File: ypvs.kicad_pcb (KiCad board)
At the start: 2 copper layers, 17 parts, among them J1 Servo, J2 LM_2596 _Input, J3 HV_Cable, J4 Motorcycle Battery, U1 Stm32f103_BluePill, U2 LM1117-3.3, U3 H11L1

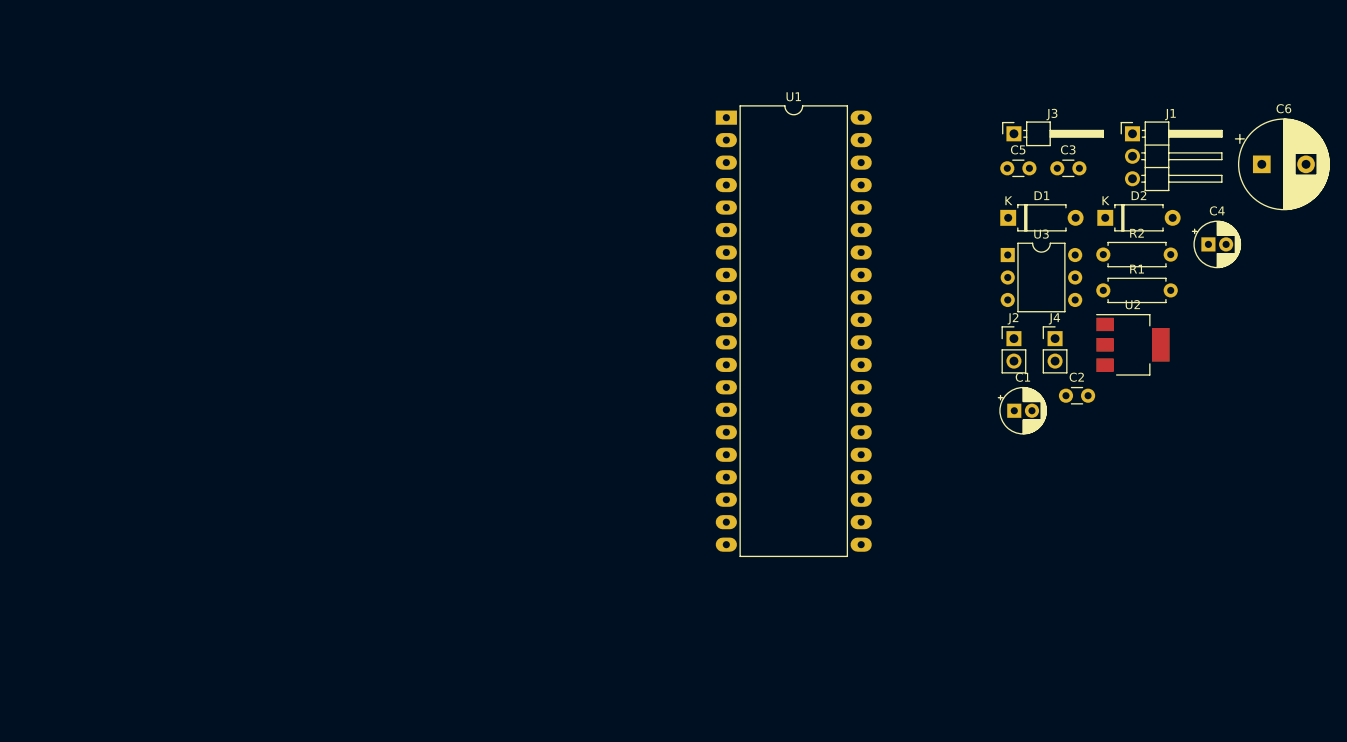
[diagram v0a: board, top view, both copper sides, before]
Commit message: added pcb outline and mounting holes
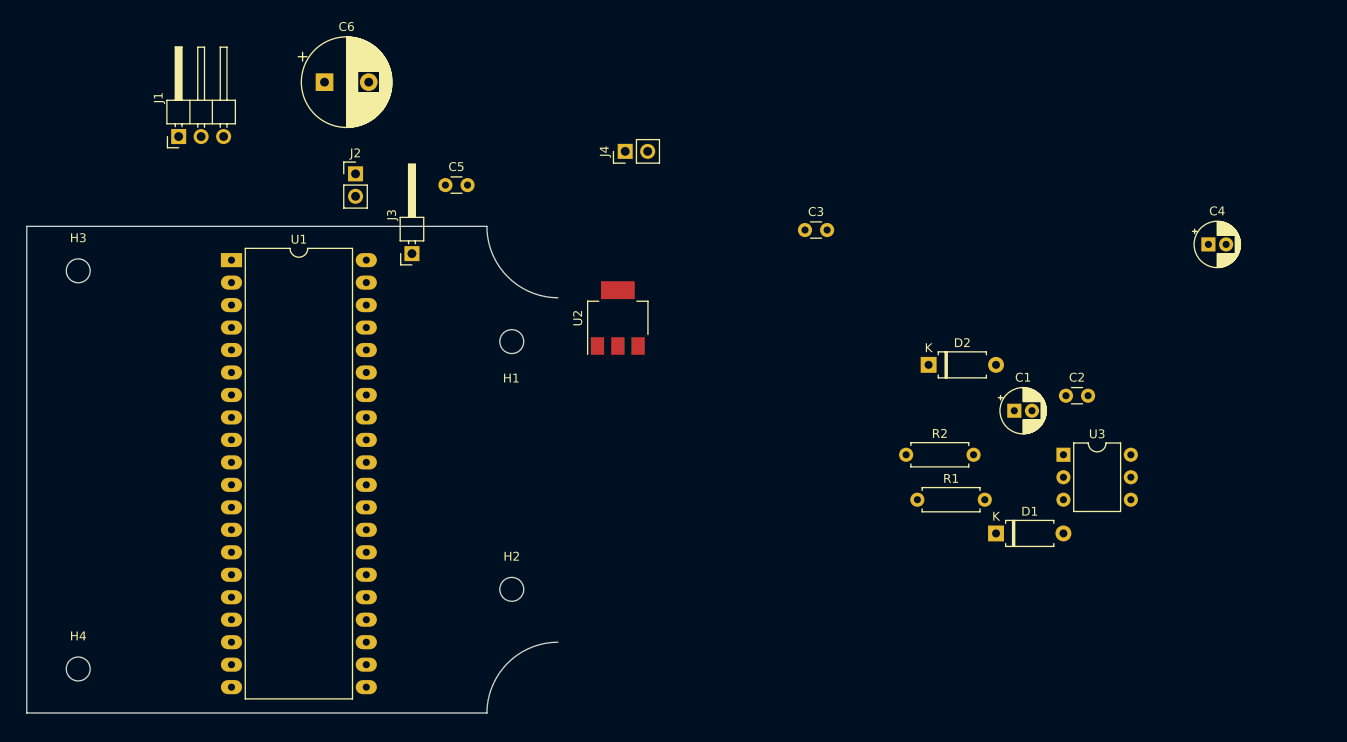
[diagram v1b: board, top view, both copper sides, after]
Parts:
- added H1: MountingHole, MountingHole:MountingHole_2.7mm_M2.5, F.Cu at (71.0, 85.0)
- added H2: MountingHole, MountingHole:MountingHole_2.7mm_M2.5, F.Cu at (71.0, 113.0)
- added H3: MountingHole, MountingHole:MountingHole_2.7mm_M2.5, F.Cu at (22.0, 77.0)
- added H4: MountingHole, MountingHole:MountingHole_2.7mm_M2.5, F.Cu at (22.0, 122.0)
- moved J1 107.8 mm to (33.4, 61.8), turned to 90 degrees
- moved C6 106.3 mm to (49.8, 55.7)
- moved J2 76.7 mm to (53.3, 66.0)
- moved J3 69.4 mm to (59.7, 75.1), turned to 90 degrees
- moved C5 63.5 mm to (63.5, 67.3)
- moved U2 58.3 mm to (83.0, 82.3), turned to 90 degrees
- moved U1 58.2 mm to (39.3, 75.8)
- moved J4 53.0 mm to (83.8, 63.5), turned to 90 degrees
- moved D1 35.7 mm to (125.7, 106.7)
- moved R2 31.8 mm to (115.6, 97.8)
- moved R1 31.6 mm to (116.8, 102.9)
- moved C3 29.4 mm to (104.1, 72.4)
- moved D2 26.0 mm to (118.1, 87.6)
- moved U3 23.4 mm to (133.3, 97.8)
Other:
- board outline added: 60 x 55 mm
- net class Default: clearance 0.2 -> 0.254; trace_width 0.25 -> 0.254; via_dia 0.8 -> 0.762; via_drill 0.4 -> 0.381
- rule trace_clearance: 0.2 -> 0.254
- rule trace_min: 0.2 -> 0.1524
- rule via_min_drill: 0.3 -> 0.3302
- rule via_min_size: 0.4 -> 0.6858

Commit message: Changed bluepill symbol
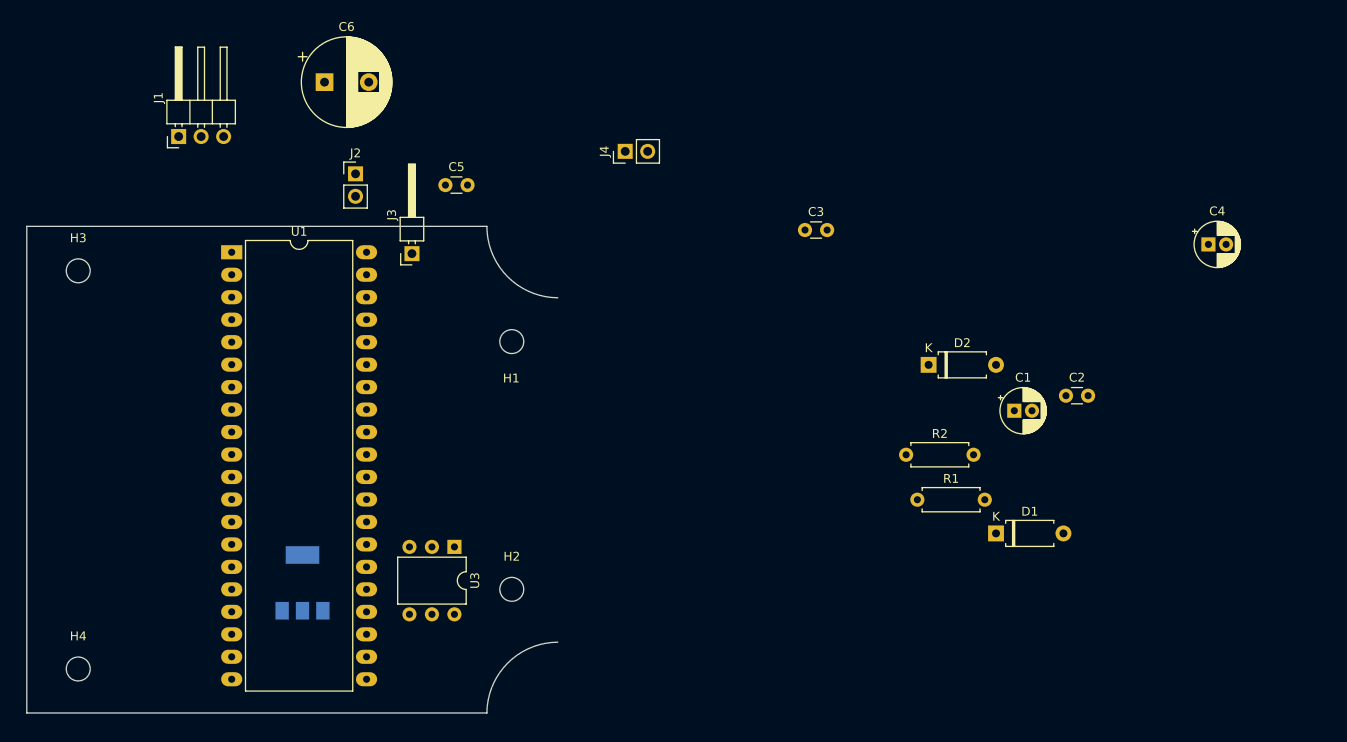
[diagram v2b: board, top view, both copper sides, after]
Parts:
- U2: moved to B.Cu
- moved U3 69.6 mm to (64.5, 108.2), turned to 270 degrees
- moved U2 46.5 mm to (47.3, 112.3)
- moved U1 0.89 mm to (39.3, 74.9)
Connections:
- U1 pad 19: GND -> Net-(U1-Pad19)
- U1 pad 20: Net-(U1-Pad20) -> +3V3
- U1 pad 23: +3V3 -> Net-(U1-Pad23)
- U1 pad 25: Net-(U1-Pad25) -> RPM_Input
- U1 pad 36: RPM_Input -> Net-(U1-Pad36)
- U1 pad 39: Net-(U1-Pad39) -> GND
- U1 pad 40: Net-(U1-Pad40) -> GND

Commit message: Added PCB traces
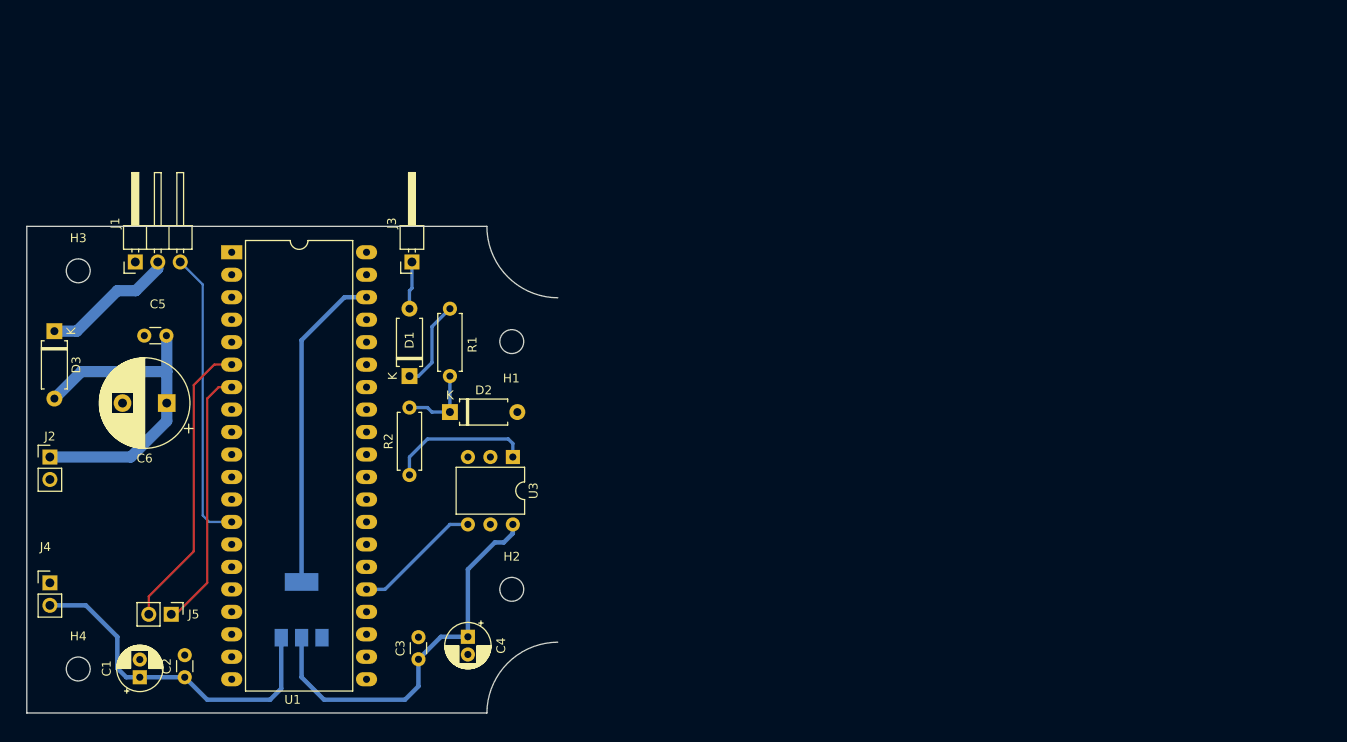
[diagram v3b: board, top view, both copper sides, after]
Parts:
- added D3: 1N4001, Diode_THT:D_A-405_P7.62mm_Horizontal, F.Cu at (19.3, 83.8)
- added J5: Debug UART, Connector_PinHeader_2.54mm:PinHeader_1x02_P2.54mm_Vertical, F.Cu at (32.5, 115.8)
- moved C2 104.6 mm to (34.0, 122.9), turned to 90 degrees
- moved C1 103.3 mm to (29.0, 122.9), turned to 90 degrees
- moved C4 94.7 mm to (66.0, 118.4), turned to 270 degrees
- moved J4 81.3 mm to (18.8, 112.3), turned to 0 degrees
- moved D1 68.6 mm to (59.4, 88.9), turned to 90 degrees
- moved C3 65.3 mm to (60.5, 120.9), turned to 90 degrees
- moved R2 56.2 mm to (59.4, 100.1), turned to 90 degrees
- moved R1 54.6 mm to (64.0, 88.9), turned to 90 degrees
- moved D2 54.4 mm to (64.0, 93.0)
- moved J2 47.1 mm to (18.8, 98.0)
- moved C6 40.4 mm to (32.0, 91.9), turned to 180 degrees
- moved C5 38.1 mm to (29.5, 84.3)
- moved J1 15.0 mm to (28.4, 76.0)
- moved U3 12.1 mm to (71.1, 98.0)
- moved U2 3.05 mm to (47.2, 115.3)
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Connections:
- J1 pad 2: +6V -> Net-(D3-Pad1)
- U1 pad 38: Net-(U1-Pad38) -> +3V3
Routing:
- net +3V3: track 0.00 -> 81.1 mm
- net +12V: track 0.00 -> 38.9 mm
- net +6V: track 0.00 -> 38.5 mm
- net Servo_PWM: track 0.00 -> 33.3 mm
- net Net-(J5-Pad2): track 0.00 -> 33.3 mm
- net Net-(J5-Pad1): track 0.00 -> 29.7 mm
- net Net-(R2-Pad1): track 0.00 -> 16.3 mm
- net Net-(D3-Pad1): track 0.00 -> 15.4 mm
- net RPM_Input: track 0.00 -> 14.5 mm
- net Net-(D1-Pad1): track 0.00 -> 10.1 mm
- net Net-(D2-Pad1): track 0.00 -> 8.85 mm
- net Net-(D1-Pad2): track 0.00 -> 5.40 mm

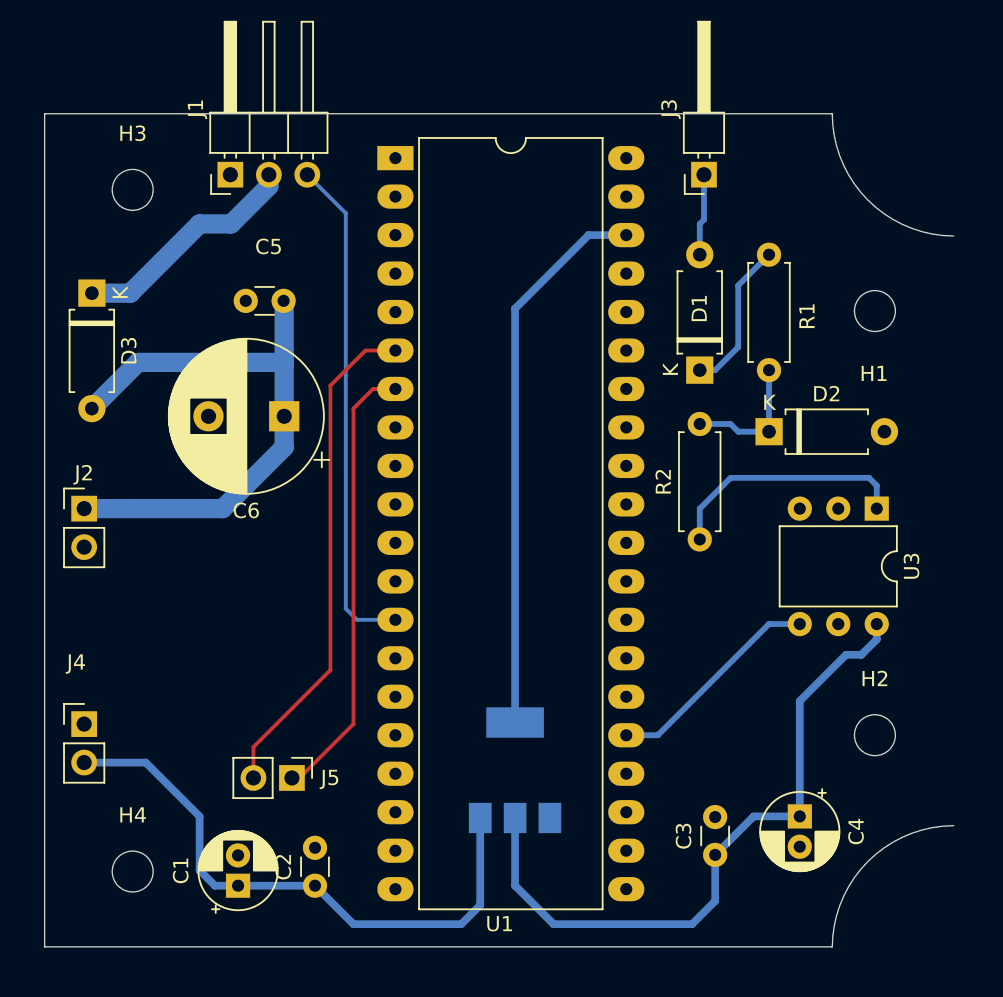
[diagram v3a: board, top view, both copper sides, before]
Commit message: Fixed outline bug, added pin labels
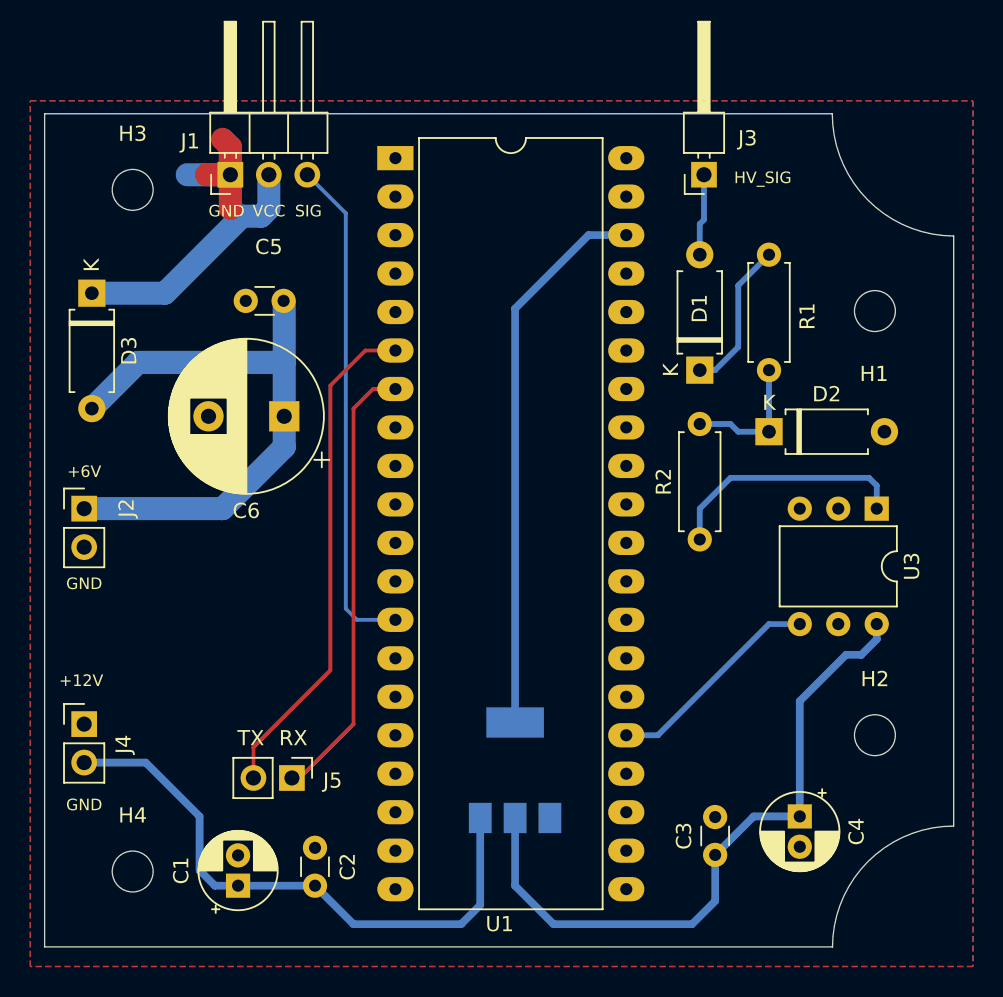
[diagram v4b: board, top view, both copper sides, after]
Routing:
- net GND: track 0.00 -> 11.0 mm
- net Net-(D3-Pad1): track 15.4 -> 16.3 mm
- added copper zone on B.Cu, net GND
- added copper zone on F.Cu, net GND
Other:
- board text added: "+12V"
- board text added: "+6V"
- board text added: "GND"
- board text added: "HV_SIG"
- board text added: "RX"
- board text added: "SIG"
- board text added: "TX"
- board text added: "VCC"
